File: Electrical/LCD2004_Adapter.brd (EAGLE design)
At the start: 100 x 55 mm, 15 parts

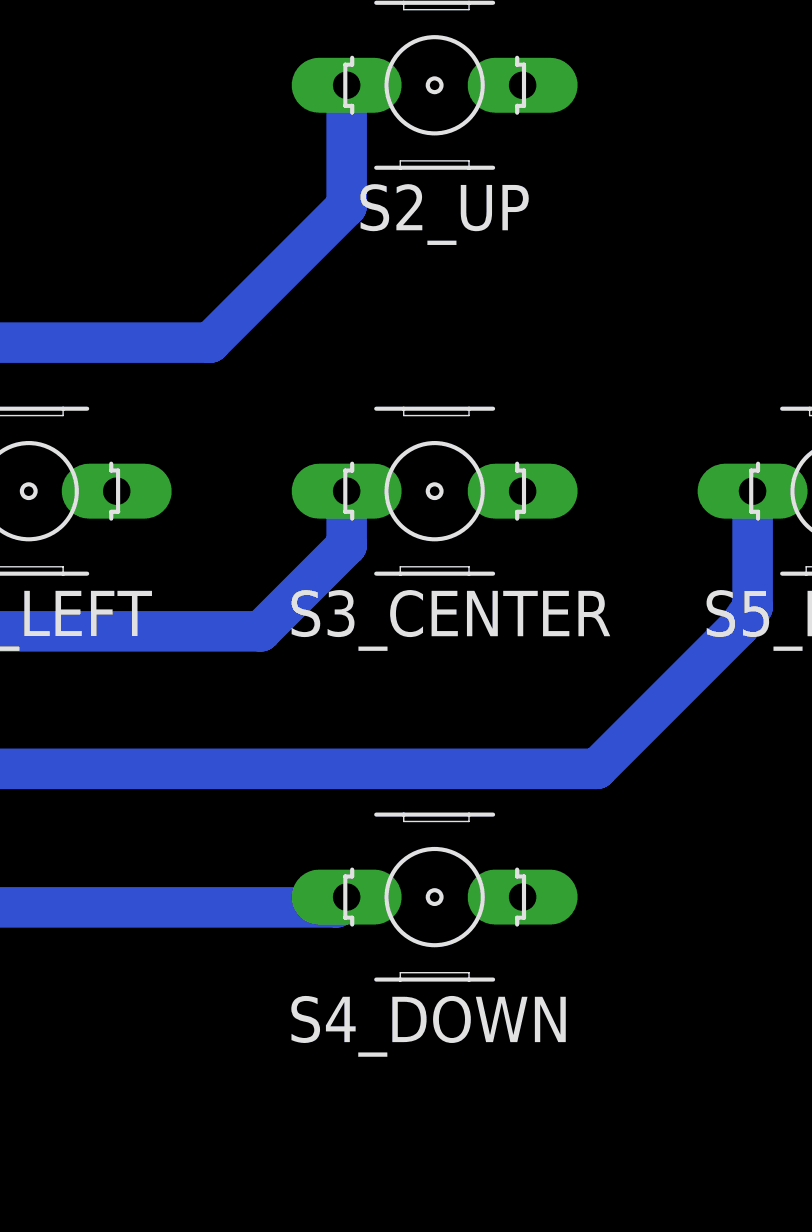
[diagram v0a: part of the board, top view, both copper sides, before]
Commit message: Swapped Up and Down buttons on PCB (making equal to Zonestar LCD)
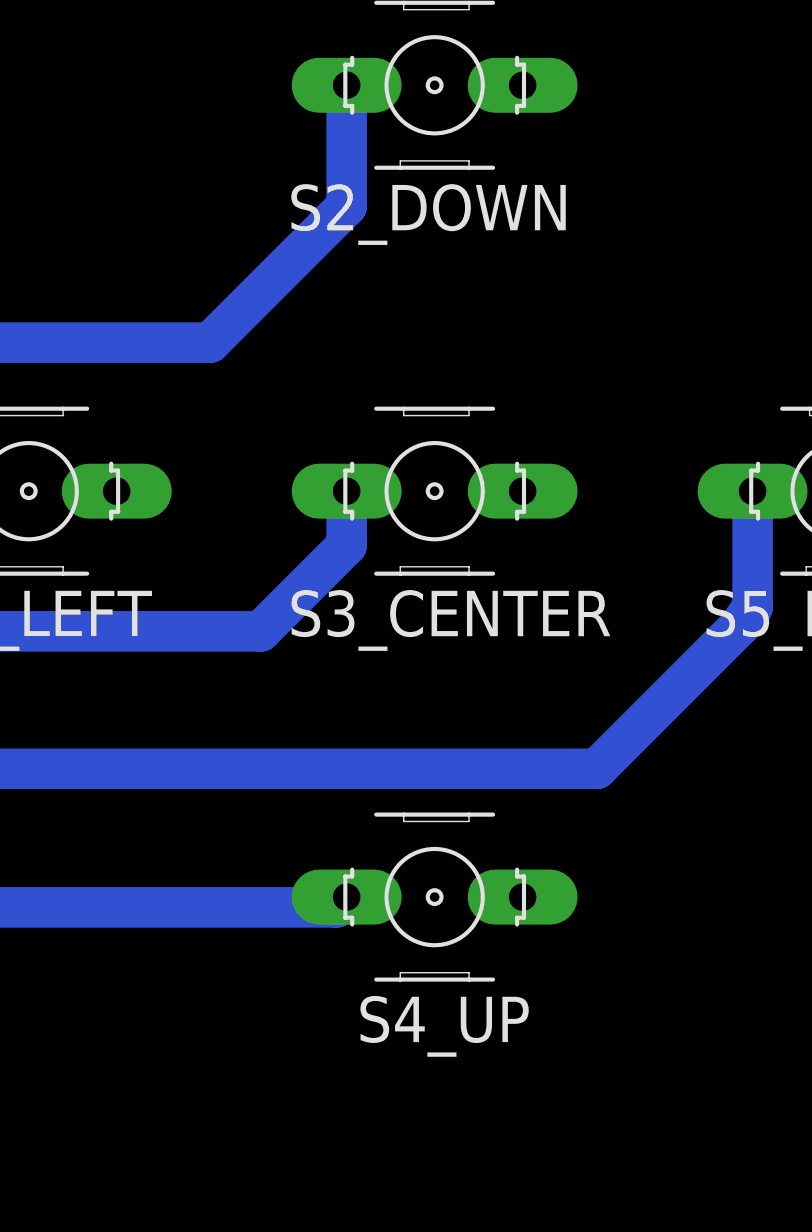
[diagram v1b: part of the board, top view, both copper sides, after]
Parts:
- R4: value 1k -> 10k
- R6: value 10k -> 1k
- renumbered S2_UP to S2_DOWN, S4_DOWN to S4_UP
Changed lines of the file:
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@@
 <drawing>
 <settings>
-<setting alwaysvectorfont="yes"/>
+<setting alwaysvectorfont="no"/>
 <setting verticaltext="up"/>
 </settings>
@@
 <attribute name="VALUE" x="71.048" y="32.58" size="1.27" layer="27" ratio="10" rot="R180"/>
 </element>
-<element name="S2_UP" library="OwnDevices" library_urn="urn:adsk.eagle:library:19498084" package="B3F-10XX" package3d_urn="urn:adsk.eagle:package:21817514/2" value="" x="83" y="42.5" smashed="yes" rot="R180">
+<element name="S2_DOWN" library="OwnDevices" library_urn="urn:adsk.eagle:library:19498084" package="B3F-10XX" package3d_urn="urn:adsk.eagle:package:21817514/2" value="" x="83" y="42.5" smashed="yes" rot="R180">
 <attribute name="MF" value="" x="83" y="42.5" size="1.778" layer="27" rot="R180" display="off"/>
-<attribute name="NAME" x="86.548" y="38.817" size="1.6764" layer="25" ratio="10" rot="R180"/>
+<attribute name="NAME" x="88.048" y="38.817" size="1.6764" layer="25" ratio="10" rot="R180"/>
 <attribute name="VALUE" x="86.048" y="47.58" size="1.27" layer="27" ratio="10" rot="R180"/>
 </element>
@@
 <attribute name="VALUE" x="86.048" y="32.58" size="1.27" layer="27" ratio="10" rot="R180"/>
 </element>
-<element name="S4_DOWN" library="OwnDevices" library_urn="urn:adsk.eagle:library:19498084" package="B3F-10XX" package3d_urn="urn:adsk.eagle:package:21817514/2" value="" x="83" y="12.5" smashed="yes" rot="R180">
+<element name="S4_UP" library="OwnDevices" library_urn="urn:adsk.eagle:library:19498084" package="B3F-10XX" package3d_urn="urn:adsk.eagle:package:21817514/2" value="" x="83" y="12.5" smashed="yes" rot="R180">
 <attribute name="MF" value="" x="83" y="12.5" size="1.778" layer="27" rot="R180" display="off"/>
-<attribute name="NAME" x="88.048" y="8.817" size="1.6764" layer="25" ratio="10" rot="R180"/>
+<attribute name="NAME" x="86.548" y="8.817" size="1.6764" layer="25" ratio="10" rot="R180"/>
 <attribute name="VALUE" x="86.048" y="17.58" size="1.27" layer="27" ratio="10" rot="R180"/>
 </element>
@@
 <attribute name="VALUE" x="55.2606" y="28.135" size="1.27" layer="27" ratio="10" rot="R180"/>
 </element>
-<element name="R4" library="rcl" library_urn="urn:adsk.eagle:library:334" package="0207/10" package3d_urn="urn:adsk.eagle:package:23491/2" value="1k" x="53" y="32.99" smashed="yes" rot="R180">
+<element name="R4" library="rcl" library_urn="urn:adsk.eagle:library:334" package="0207/10" package3d_urn="urn:adsk.eagle:package:23491/2" value="10k" x="53" y="32.99" smashed="yes" rot="R180">
 <attribute name="NAME" x="56.048" y="31.466" size="1.6764" layer="25" ratio="10" rot="R180"/>
 <attribute name="POPULARITY" value="81" x="53" y="32.99" size="1.778" layer="27" rot="R180" display="off"/>
@@
 <attribute name="VALUE" x="55.2606" y="22.955" size="1.27" layer="27" ratio="10" rot="R180"/>
 </element>
-<element name="R6" library="rcl" library_urn="urn:adsk.eagle:library:334" package="0207/10" package3d_urn="urn:adsk.eagle:package:23491/2" value="10k" x="53" y="12.12" smashed="yes" rot="R180">
+<element name="R6" library="rcl" library_urn="urn:adsk.eagle:library:334" package="0207/10" package3d_urn="urn:adsk.eagle:package:23491/2" value="1k" x="53" y="12.12" smashed="yes" rot="R180">
 <attribute name="NAME" x="56.048" y="10.596" size="1.6764" layer="25" ratio="10" rot="R180"/>
 <attribute name="POPULARITY" value="81" x="53" y="12.12" size="1.778" layer="27" rot="R180" display="off"/>
@@
 <signal name="N$4">
 <contactref element="R4" pad="1"/>
-<contactref element="S2_UP" pad="2"/>
+<contactref element="S2_DOWN" pad="2"/>
 <wire x1="79.7488" y1="38.0388" x2="74.7" y2="32.99" width="1.5" layer="16"/>
 <wire x1="58.08" y1="32.99" x2="74.7" y2="32.99" width="1.5" layer="16"/>
@@
 <signal name="N$6">
 <contactref element="R6" pad="1"/>
-<contactref element="S4_DOWN" pad="2"/>
+<contactref element="S4_UP" pad="2"/>
 <wire x1="79.7488" y1="12.5" x2="79.3688" y2="12.12" width="1.5" layer="16"/>
 <wire x1="58.08" y1="12.12" x2="79.3688" y2="12.12" width="1.5" layer="16"/>
@@
 <contactref element="S1_LEFT" pad="1"/>
 <contactref element="S5_RIGHT" pad="1"/>
-<contactref element="S2_UP" pad="1"/>
+<contactref element="S2_DOWN" pad="1"/>
 <contactref element="S3_CENTER" pad="1"/>
-<contactref element="S4_DOWN" pad="1"/>
+<contactref element="S4_UP" pad="1"/>
 <contactref element="D1" pad="A"/>
 <contactref element="J3_LCD" pad="2"/>
